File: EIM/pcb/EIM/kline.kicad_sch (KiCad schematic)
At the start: 8 parts, among them IC1 TLIN1027DRQ1

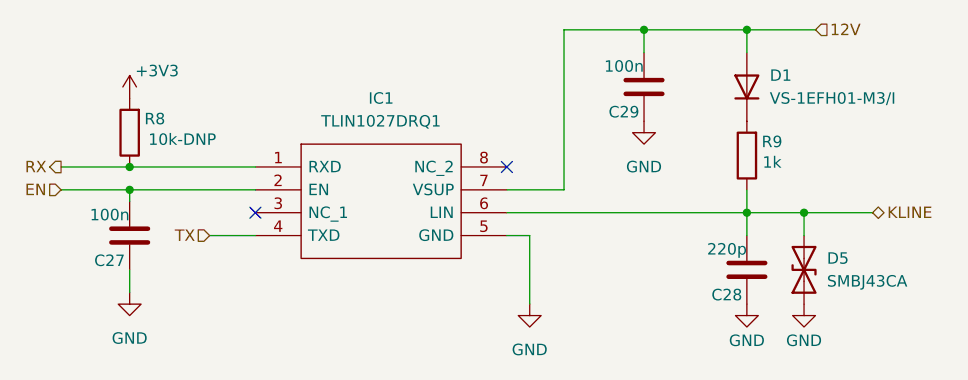
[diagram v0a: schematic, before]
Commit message: added Arjun's comments, assigned some MCU pins
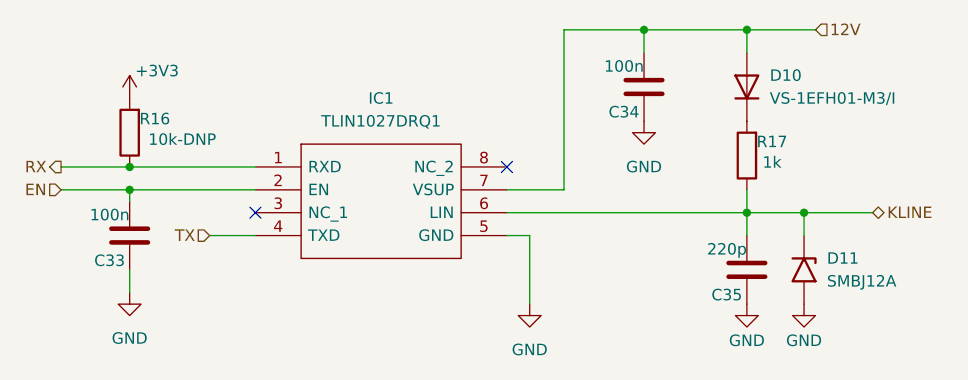
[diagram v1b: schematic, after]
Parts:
- removed D5: SMBJ43CA, Diode_SMD:D_SMB, symbol Device:D_TVS
- added D11: SMBJ12A, Diode_SMD:D_SMB, symbol Diode:SM6T10A
- renumbered C27 to C33, C29 to C34, C28 to C35, D1 to D10, R8 to R16, R9 to R17
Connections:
- net GND: now also D11.2 (A2)
- net KLINE: now also D11.1 (A1)
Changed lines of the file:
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@@
 		(on_board yes)
 		(dnp no)
-		(property "Reference" "#PWR046"
+		(property "Reference" "#PWR084"
 			(at 186.69 113.03 0)
 			(effects
@@
 			(project "EIM"
 				(path "/2e0b3b3d-5537-41dc-9fad-4fb33afdbfad/08df7d8f-6781-4b98-a316-f1c5c896db59"
-					(reference "#PWR046")
+					(reference "#PWR084")
 					(unit 1)
 				)
@@
 		(dnp no)
 		(fields_autoplaced yes)
-		(property "Reference" "#PWR043"
+		(property "Reference" "#PWR082"
 			(at 162.56 113.03 0)
 			(effects
@@
 			(project ""
 				(path "/2e0b3b3d-5537-41dc-9fad-4fb33afdbfad/08df7d8f-6781-4b98-a316-f1c5c896db59"
-					(reference "#PWR043")
+					(reference "#PWR082")
 					(unit 1)
 				)
@@
 		(on_board yes)
 		(dnp no)
-		(property "Reference" "#PWR045"
+		(property "Reference" "#PWR080"
 			(at 118.11 87.63 0)
 			(effects
@@
 			(project "EIM"
 				(path "/2e0b3b3d-5537-41dc-9fad-4fb33afdbfad/08df7d8f-6781-4b98-a316-f1c5c896db59"
-					(reference "#PWR045")
+					(reference "#PWR080")
 					(unit 1)
 				)
@@
 		(on_board yes)
 		(dnp no)
-		(property "Reference" "C29"
+		(property "Reference" "C34"
 			(at 174.752 85.344 0)
 			(effects
@@
 			(project "EIM"
 				(path "/2e0b3b3d-5537-41dc-9fad-4fb33afdbfad/08df7d8f-6781-4b98-a316-f1c5c896db59"
-					(reference "C29")
+					(reference "C34")
 					(unit 1)
 				)
@@
 		(dnp no)
 		(fields_autoplaced yes)
-		(property "Reference" "#PWR044"
+		(property "Reference" "#PWR081"
 			(at 118.11 111.76 0)
 			(effects
@@
 			(project "EIM"
 				(path "/2e0b3b3d-5537-41dc-9fad-4fb33afdbfad/08df7d8f-6781-4b98-a316-f1c5c896db59"
-					(reference "#PWR044")
-					(unit 1)
-				)
-			)
-		)
-	)
-	(symbol
-		(lib_id "Device:D_TVS")
-		(at 193.04 102.87 90)
-		(unit 1)
-		(exclude_from_sim no)
-		(in_bom yes)
-		(on_board yes)
-		(dnp no)
-		(fields_autoplaced yes)
-		(property "Reference" "D5"
-			(at 195.58 101.5999 90)
-			(effects
-				(font
-					(size 1.27 1.27)
-				)
-				(justify right)
-			)
-		)
-		(property "Value" "SMBJ43CA"
-			(at 195.58 104.1399 90)
-			(effects
-				(font
-					(size 1.27 1.27)
-				)
-				(justify right)
-			)
-		)
-		(property "Footprint" "Diode_SMD:D_SMB"
-			(at 193.04 102.87 0)
-			(effects
-				(font
-					(size 1.27 1.27)
-				)
-				(hide yes)
-			)
-		)
-		(property "Datasheet" "~"
-			(at 193.04 102.87 0)
-			(effects
-				(font
-					(size 1.27 1.27)
-				)
-				(hide yes)
-			)
-		)
-		(property "Description" "Bidirectional transient-voltage-suppression diode"
-			(at 193.04 102.87 0)
-			(effects
-				(font
-					(size 1.27 1.27)
-				)
-				(hide yes)
-			)
-		)
-		(pin "2"
-		)
-		(pin "1"
-		)
-		(instances
-			(project ""
-				(path "/2e0b3b3d-5537-41dc-9fad-4fb33afdbfad/08df7d8f-6781-4b98-a316-f1c5c896db59"
-					(reference "D5")
+					(reference "#PWR081")
 					(unit 1)
 				)
@@
 		(on_board yes)
 		(dnp no)
-		(property "Reference" "C28"
+		(property "Reference" "C35"
 			(at 186.182 105.664 0)
 			(effects
@@
 			(project "EIM"
 				(path "/2e0b3b3d-5537-41dc-9fad-4fb33afdbfad/08df7d8f-6781-4b98-a316-f1c5c896db59"
-					(reference "C28")
+					(reference "C35")
+					(unit 1)
+				)
+			)
+		)
+	)
+	(symbol
+		(lib_id "Diode:SM6T10A")
+		(at 193.04 102.87 270)
+		(unit 1)
+		(exclude_from_sim no)
+		(in_bom yes)
+		(on_board yes)
+		(dnp no)
+		(property "Reference" "D11"
+			(at 195.58 101.5999 90)
+			(effects
+				(font
+					(size 1.27 1.27)
+				)
+				(justify left)
+			)
+		)
+		(property "Value" "SMBJ12A"
+			(at 195.58 104.1399 90)
+			(effects
+				(font
+					(size 1.27 1.27)
+				)
+				(justify left)
+			)
+		)
+		(property "Footprint" "Diode_SMD:D_SMB"
+			(at 187.96 102.87 0)
+			(effects
+				(font
+					(size 1.27 1.27)
+				)
+				(hide yes)
+			)
+		)
+		(property "Datasheet" "https://www.st.com/resource/en/datasheet/sm6t.pdf"
+			(at 193.04 101.6 0)
+			(effects
+				(font
+					(size 1.27 1.27)
+				)
+				(hide yes)
+			)
+		)
+		(property "Description" "600W unidirectional Transil Transient Voltage Suppressor, 10Vrwm, DO-214AA"
+			(at 193.04 102.87 0)
+			(effects
+				(font
+					(size 1.27 1.27)
+				)
+				(hide yes)
+			)
+		)
+		(pin "1"
+		)
+		(pin "2"
+		)
+		(instances
+			(project "EIM"
+				(path "/2e0b3b3d-5537-41dc-9fad-4fb33afdbfad/08df7d8f-6781-4b98-a316-f1c5c896db59"
+					(reference "D11")
 					(unit 1)
 				)
@@
 		(on_board yes)
 		(dnp no)
-		(property "Reference" "R9"
+		(property "Reference" "R17"
 			(at 189.484 88.646 0)
 			(effects
@@
 			(project "EIM"
 				(path "/2e0b3b3d-5537-41dc-9fad-4fb33afdbfad/08df7d8f-6781-4b98-a316-f1c5c896db59"
-					(reference "R9")
+					(reference "R17")
 					(unit 1)
 				)
@@
 		(dnp no)
 		(fields_autoplaced yes)
-		(property "Reference" "D1"
+		(property "Reference" "D10"
 			(at 189.23 81.2799 90)
 			(effects
@@
 			(project ""
 				(path "/2e0b3b3d-5537-41dc-9fad-4fb33afdbfad/08df7d8f-6781-4b98-a316-f1c5c896db59"
-					(reference "D1")
+					(reference "D10")
 					(unit 1)
 				)
@@
 		(on_board yes)
 		(dnp no)
-		(property "Reference" "#PWR056"
+		(property "Reference" "#PWR085"
 			(at 193.04 113.03 0)
 			(effects
@@
 			(project "EIM"
 				(path "/2e0b3b3d-5537-41dc-9fad-4fb33afdbfad/08df7d8f-6781-4b98-a316-f1c5c896db59"
-					(reference "#PWR056")
+					(reference "#PWR085")
 					(unit 1)
 				)
@@
 		(dnp no)
 		(fields_autoplaced yes)
-		(property "Reference" "#PWR047"
+		(property "Reference" "#PWR083"
 			(at 175.26 92.71 0)
 			(effects
@@
 			(project "EIM"
 				(path "/2e0b3b3d-5537-41dc-9fad-4fb33afdbfad/08df7d8f-6781-4b98-a316-f1c5c896db59"
-					(reference "#PWR047")
+					(reference "#PWR083")
 					(unit 1)
 				)
@@
 		(on_board yes)
 		(dnp no)
-		(property "Reference" "C27"
+		(property "Reference" "C33"
 			(at 117.602 101.854 0)
 			(effects
@@
 			(project "EIM"
 				(path "/2e0b3b3d-5537-41dc-9fad-4fb33afdbfad/08df7d8f-6781-4b98-a316-f1c5c896db59"
-					(reference "C27")
+					(reference "C33")
 					(unit 1)
 				)
@@
 		(on_board yes)
 		(dnp no)
-		(property "Reference" "R8"
+		(property "Reference" "R16"
 			(at 120.904 86.106 0)
 			(effects
@@
 			(project "EIM"
 				(path "/2e0b3b3d-5537-41dc-9fad-4fb33afdbfad/08df7d8f-6781-4b98-a316-f1c5c896db59"
-					(reference "R8")
-					(unit 1)
-				)
+					(reference "R16")
+					(unit 1)
+				)

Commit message: Layout 75% done, before 8V bus deletion
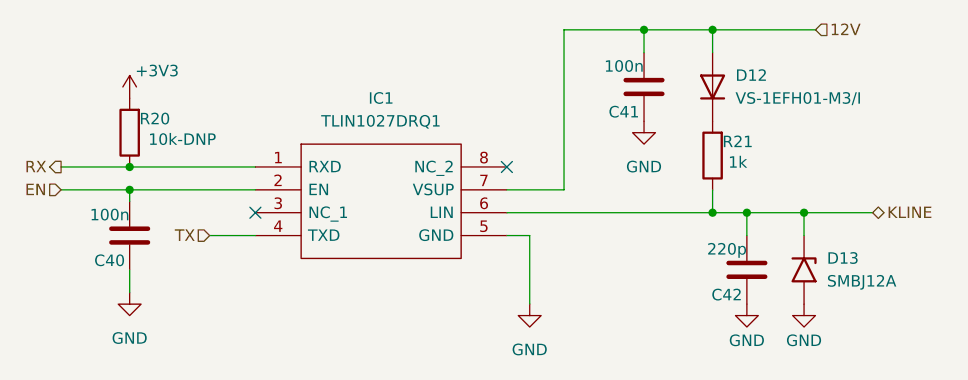
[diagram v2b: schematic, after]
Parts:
- renumbered C33 to C40, C34 to C41, C35 to C42, D10 to D12, D11 to D13, R16 to R20, R17 to R21
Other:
- moved on the sheet: D12, R21
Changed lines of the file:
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@@
 	(paper "A4")
+	(junction
+		(at 182.88 96.52)
+		(diameter 0)
+		(color 0 0 0 0)
+	)
 	(junction
 		(at 118.11 93.98)
@@
 	)
 	(junction
-		(at 186.69 76.2)
+		(at 182.88 76.2)
 		(diameter 0)
 		(color 0 0 0 0)
@@
 	(wire
 		(pts
-			(xy 160.02 96.52) (xy 186.69 96.52)
-		)
-		(stroke
-			(width 0)
-			(type default)
-		)
-	)
-	(wire
-		(pts
-			(xy 175.26 76.2) (xy 186.69 76.2)
+			(xy 160.02 96.52) (xy 182.88 96.52)
+		)
+		(stroke
+			(width 0)
+			(type default)
+		)
+	)
+	(wire
+		(pts
+			(xy 175.26 76.2) (xy 182.88 76.2)
 		)
 		(stroke
@@
 	(wire
 		(pts
+			(xy 182.88 96.52) (xy 186.69 96.52)
+		)
+		(stroke
+			(width 0)
+			(type default)
+		)
+	)
+	(wire
+		(pts
+			(xy 182.88 76.2) (xy 194.31 76.2)
+		)
+		(stroke
+			(width 0)
+			(type default)
+		)
+	)
+	(wire
+		(pts
 			(xy 118.11 91.44) (xy 132.08 91.44)
 		)
@@
 	(wire
 		(pts
-			(xy 186.69 93.98) (xy 186.69 96.52)
-		)
-		(stroke
-			(width 0)
-			(type default)
-		)
-	)
-	(wire
-		(pts
-			(xy 186.69 78.74) (xy 186.69 76.2)
+			(xy 182.88 93.98) (xy 182.88 96.52)
+		)
+		(stroke
+			(width 0)
+			(type default)
+		)
+	)
+	(wire
+		(pts
+			(xy 182.88 78.74) (xy 182.88 76.2)
 		)
 		(stroke
@@
 		(pts
 			(xy 162.56 99.06) (xy 162.56 106.68)
-		)
-		(stroke
-			(width 0)
-			(type default)
-		)
-	)
-	(wire
-		(pts
-			(xy 186.69 76.2) (xy 194.31 76.2)
 		)
 		(stroke
@@
 		(on_board yes)
 		(dnp no)
-		(property "Reference" "#PWR084"
+		(property "Reference" "#PWR093"
 			(at 186.69 113.03 0)
 			(effects
@@
 			(project "EIM"
 				(path "/2e0b3b3d-5537-41dc-9fad-4fb33afdbfad/08df7d8f-6781-4b98-a316-f1c5c896db59"
-					(reference "#PWR084")
+					(reference "#PWR093")
 					(unit 1)
 				)
@@
 		(dnp no)
 		(fields_autoplaced yes)
-		(property "Reference" "#PWR082"
+		(property "Reference" "#PWR091"
 			(at 162.56 113.03 0)
 			(effects
@@
 			(project ""
 				(path "/2e0b3b3d-5537-41dc-9fad-4fb33afdbfad/08df7d8f-6781-4b98-a316-f1c5c896db59"
-					(reference "#PWR082")
+					(reference "#PWR091")
 					(unit 1)
 				)
@@
 		(on_board yes)
 		(dnp no)
-		(property "Reference" "#PWR080"
+		(property "Reference" "#PWR089"
 			(at 118.11 87.63 0)
 			(effects
@@
 			(project "EIM"
 				(path "/2e0b3b3d-5537-41dc-9fad-4fb33afdbfad/08df7d8f-6781-4b98-a316-f1c5c896db59"
-					(reference "#PWR080")
+					(reference "#PWR089")
 					(unit 1)
 				)
@@
 		(on_board yes)
 		(dnp no)
-		(property "Reference" "C34"
+		(property "Reference" "C41"
 			(at 174.752 85.344 0)
 			(effects
@@
 			(project "EIM"
 				(path "/2e0b3b3d-5537-41dc-9fad-4fb33afdbfad/08df7d8f-6781-4b98-a316-f1c5c896db59"
-					(reference "C34")
+					(reference "C41")
 					(unit 1)
 				)
@@
 		(dnp no)
 		(fields_autoplaced yes)
-		(property "Reference" "#PWR081"
+		(property "Reference" "#PWR090"
 			(at 118.11 111.76 0)
 			(effects
@@
 			(project "EIM"
 				(path "/2e0b3b3d-5537-41dc-9fad-4fb33afdbfad/08df7d8f-6781-4b98-a316-f1c5c896db59"
-					(reference "#PWR081")
+					(reference "#PWR090")
 					(unit 1)
 				)
@@
 		(on_board yes)
 		(dnp no)
-		(property "Reference" "C35"
+		(property "Reference" "C42"
 			(at 186.182 105.664 0)
 			(effects
@@
 			(project "EIM"
 				(path "/2e0b3b3d-5537-41dc-9fad-4fb33afdbfad/08df7d8f-6781-4b98-a316-f1c5c896db59"
-					(reference "C35")
+					(reference "C42")
 					(unit 1)
 				)
@@
 		(on_board yes)
 		(dnp no)
-		(property "Reference" "D11"
+		(property "Reference" "D13"
 			(at 195.58 101.5999 90)
 			(effects
@@
 			(project "EIM"
 				(path "/2e0b3b3d-5537-41dc-9fad-4fb33afdbfad/08df7d8f-6781-4b98-a316-f1c5c896db59"
-					(reference "D11")
+					(reference "D13")
 					(unit 1)
 				)
@@
 	(symbol
 		(lib_id "Device:R")
-		(at 186.69 90.17 180)
+		(at 182.88 90.17 180)
 		(unit 1)
 		(exclude_from_sim no)
@@
 		(on_board yes)
 		(dnp no)
-		(property "Reference" "R17"
-			(at 189.484 88.646 0)
+		(property "Reference" "R21"
+			(at 185.674 88.646 0)
 			(effects
 				(font
@@
 		)
 		(property "Value" "1k"
-			(at 189.484 90.932 0)
+			(at 185.674 90.932 0)
 			(effects
 				(font
@@
 		)
 		(property "Footprint" "Resistor_SMD:R_0805_2012Metric_Pad1.20x1.40mm_HandSolder"
-			(at 188.468 90.17 90)
+			(at 184.658 90.17 90)
 			(effects
 				(font
@@
 		)
 		(property "Datasheet" "~"
-			(at 186.69 90.17 0)
+			(at 182.88 90.17 0)
 			(effects
 				(font
@@
 		)
 		(property "Description" "Resistor"
-			(at 186.69 90.17 0)
+			(at 182.88 90.17 0)
 			(effects
 				(font
@@
 			(project "EIM"
 				(path "/2e0b3b3d-5537-41dc-9fad-4fb33afdbfad/08df7d8f-6781-4b98-a316-f1c5c896db59"
-					(reference "R17")
+					(reference "R21")
 					(unit 1)
 				)
@@
 	(symbol
 		(lib_id "Device:D")
-		(at 186.69 82.55 90)
+		(at 182.88 82.55 90)
 		(unit 1)
 		(exclude_from_sim no)
@@
 		(dnp no)
 		(fields_autoplaced yes)
-		(property "Reference" "D10"
-			(at 189.23 81.2799 90)
+		(property "Reference" "D12"
+			(at 185.42 81.2799 90)
 			(effects
 				(font
@@
 		)
 		(property "Value" "VS-1EFH01-M3/I"
-			(at 189.23 83.8199 90)
+			(at 185.42 83.8199 90)
 			(effects
 				(font
@@
 		)
 		(property "Footprint" "Diode_SMD:D_SMF"
-			(at 186.69 82.55 0)
+			(at 182.88 82.55 0)
 			(effects
 				(font
@@
 		)
 		(property "Datasheet" "~"
-			(at 186.69 82.55 0)
+			(at 182.88 82.55 0)
 			(effects
 				(font
@@
 		)
 		(property "Description" "Diode"
-			(at 186.69 82.55 0)
+			(at 182.88 82.55 0)
 			(effects
 				(font
@@
 		)
 		(property "Sim.Device" "D"
-			(at 186.69 82.55 0)
+			(at 182.88 82.55 0)
 			(effects
 				(font
@@
 		)
 		(property "Sim.Pins" "1=K 2=A"
-			(at 186.69 82.55 0)
+			(at 182.88 82.55 0)
 			(effects
 				(font
@@
 			(project ""
 				(path "/2e0b3b3d-5537-41dc-9fad-4fb33afdbfad/08df7d8f-6781-4b98-a316-f1c5c896db59"
-					(reference "D10")
+					(reference "D12")
 					(unit 1)
 				)
@@
 		(on_board yes)
 		(dnp no)
-		(property "Reference" "#PWR085"
+		(property "Reference" "#PWR094"
 			(at 193.04 113.03 0)
 			(effects
@@
 			(project "EIM"
 				(path "/2e0b3b3d-5537-41dc-9fad-4fb33afdbfad/08df7d8f-6781-4b98-a316-f1c5c896db59"
-					(reference "#PWR085")
+					(reference "#PWR094")
 					(unit 1)
 				)
@@
 		(dnp no)
 		(fields_autoplaced yes)
-		(property "Reference" "#PWR083"
+		(property "Reference" "#PWR092"
 			(at 175.26 92.71 0)
 			(effects
@@
 			(project "EIM"
 				(path "/2e0b3b3d-5537-41dc-9fad-4fb33afdbfad/08df7d8f-6781-4b98-a316-f1c5c896db59"
-					(reference "#PWR083")
+					(reference "#PWR092")
 					(unit 1)
 				)
@@
 		(on_board yes)
 		(dnp no)
-		(property "Reference" "C33"
+		(property "Reference" "C40"
 			(at 117.602 101.854 0)
 			(effects
@@
 			(project "EIM"
 				(path "/2e0b3b3d-5537-41dc-9fad-4fb33afdbfad/08df7d8f-6781-4b98-a316-f1c5c896db59"
-					(reference "C33")
+					(reference "C40")
 					(unit 1)
 				)
@@
 		(on_board yes)
 		(dnp no)
-		(property "Reference" "R16"
+		(property "Reference" "R20"
 			(at 120.904 86.106 0)
 			(effects
@@
 			(project "EIM"
 				(path "/2e0b3b3d-5537-41dc-9fad-4fb33afdbfad/08df7d8f-6781-4b98-a316-f1c5c896db59"
-					(reference "R16")
+					(reference "R20")
 					(unit 1)
 				)
